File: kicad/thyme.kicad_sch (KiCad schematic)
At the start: 86 parts, among them SW1 SW_Push, SW10 SW_Push, SW11 SW_Push, SW12 SW_Push, SW13 SW_Push, SW14 SW_Push, SW15 SW_Push, SW16 SW_Push, SW17 SW_Push, SW18 SW_Push, SW19 SW_Push, SW2 SW_Push, SW20 SW_Push, SW21 SW_Push, SW22 SW_Push, SW23 SW_Push, SW24 SW_Push, SW25 SW_Push, SW26 SW_Push, SW27 SW_Push, SW28 SW_Push, SW29 SW_Push, SW3 SW_Push, SW30 SW_Push, SW31 SW_Push, SW32 SW_Push, SW33 SW_Push, SW34 SW_Push, SW35 SW_Push, SW36 SW_Push, SW37 SW_Push, SW38 SW_Push, SW39 SW_Push, SW4 SW_Push, SW40 SW_Push, SW41 SW_Push, SW42 SW_Push, SW5 SW_Push, SW6 SW_Push, SW7 SW_Push, SW8 SW_Push, SW9 SW_Push, U1 nice_nano, U2 nice_nano

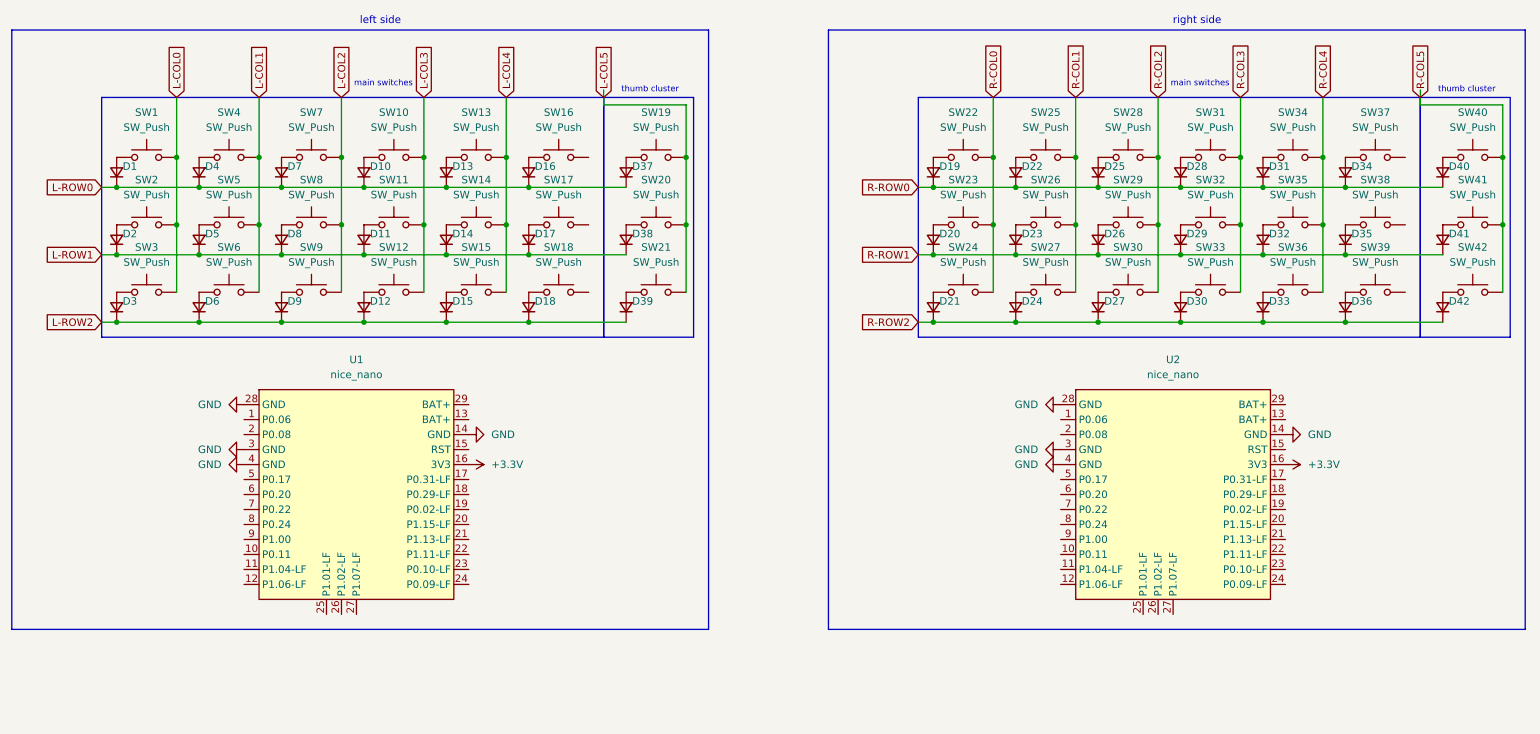
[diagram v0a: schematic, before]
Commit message: feat: add the jst power connections and connect nets
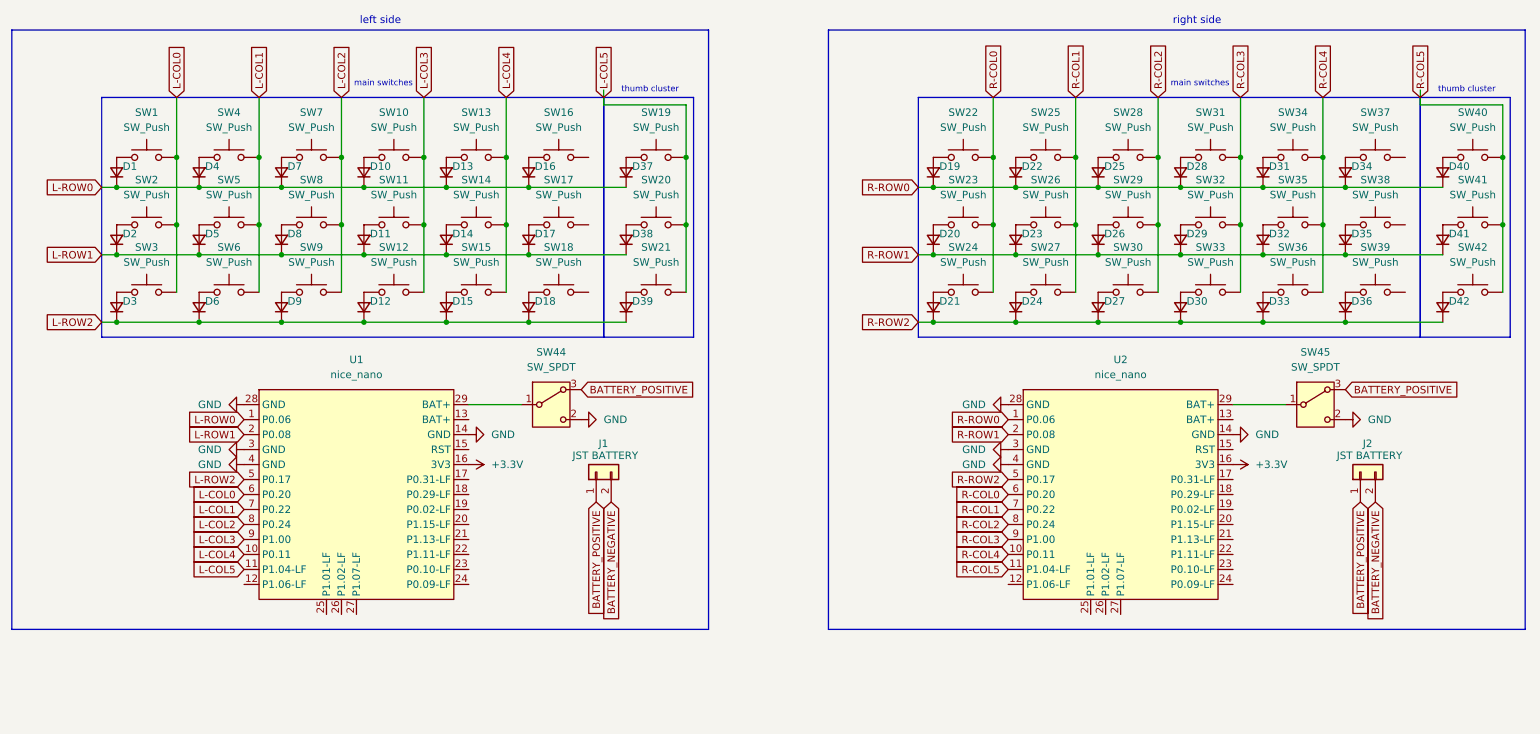
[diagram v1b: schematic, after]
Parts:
- added J1, J2: JST BATTERY, Connector_JST:JST_PH_B2B-PH-K_1x02_P2.00mm_Vertical, symbol Connector_Generic:Conn_01x02
- added SW44, SW45: SW_SPDT, Button_Switch_THT:SW_Slide-03_Wuerth-WS-SLTV_10x2.5x6.4_P2.54mm, symbol Switch:SW_Wuerth_450301014042
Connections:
- net GND: now also SW44.2 (C), SW45.2 (C)
- net L-COL0: now also U1.6 (P0.20)
- net L-COL1: now also U1.7 (P0.22)
- net L-COL2: now also U1.8 (P0.24)
- net L-COL3: now also U1.9 (P1.00)
- net L-COL4: now also U1.10 (P0.11)
- net L-COL5: now also U1.11 (P1.04-LF)
- net L-ROW0: now also U1.1 (P0.06)
- net L-ROW1: now also U1.2 (P0.08)
- net L-ROW2: now also U1.5 (P0.17)
- net R-COL0: now also U2.6 (P0.20)
- net R-COL1: now also U2.7 (P0.22)
- net R-COL2: now also U2.8 (P0.24)
- net R-COL3: now also U2.9 (P1.00)
- net R-COL4: now also U2.10 (P0.11)
- net R-COL5: now also U2.11 (P1.04-LF)
- net R-ROW0: now also U2.1 (P0.06)
- net R-ROW1: now also U2.2 (P0.08)
- net R-ROW2: now also U2.5 (P0.17)
- net at U1.29 (BAT+): now also SW44.1 (B)
- net at U2.29 (BAT+): now also SW45.1 (B)
- new net BATTERY_NEGATIVE: J1.2 (Pin_2), J2.2 (Pin_2)
- new net BATTERY_POSITIVE: J1.1 (Pin_1), J2.1 (Pin_1), SW44.3 (A), SW45.3 (A)

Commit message: bug: fix row 5 being unconnected
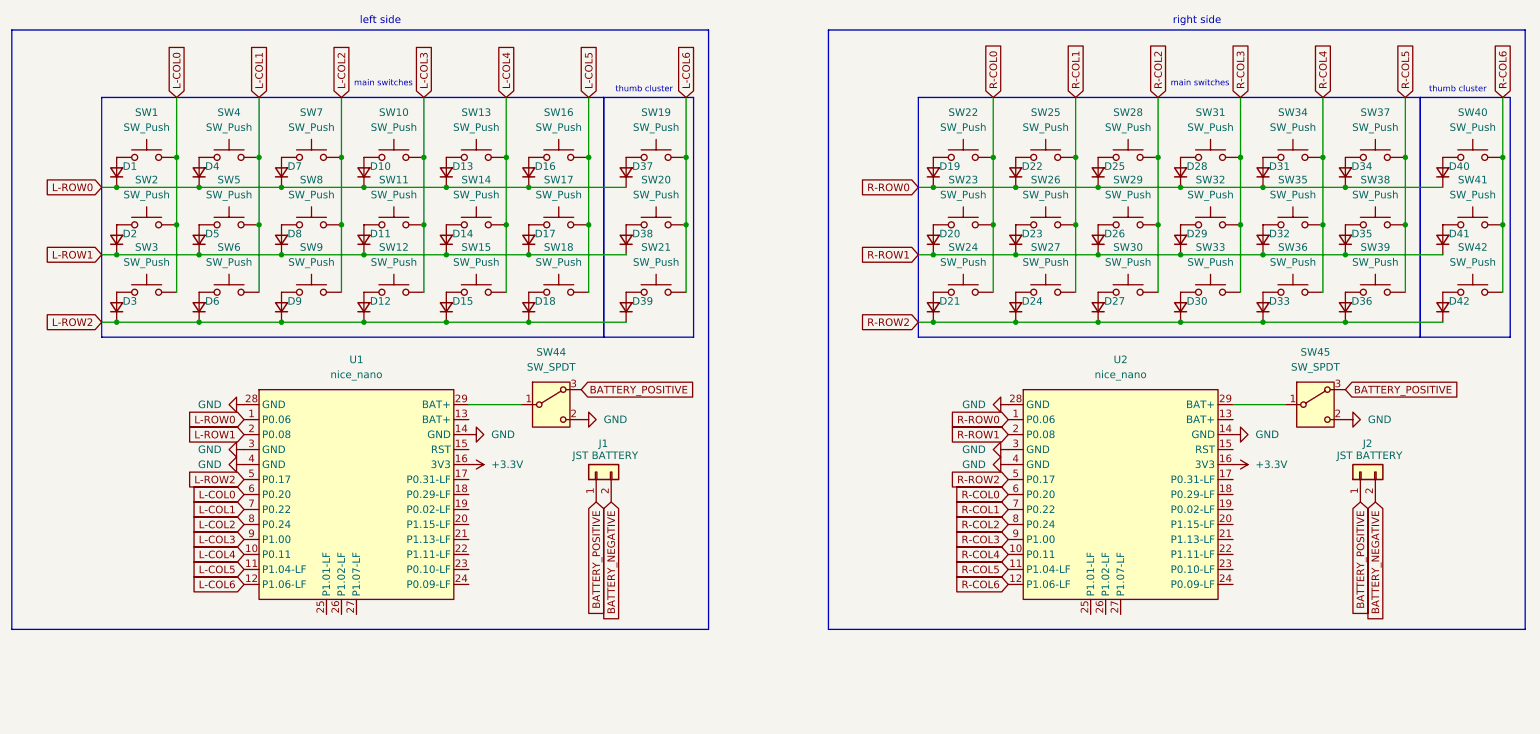
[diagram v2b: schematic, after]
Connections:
- net L-COL5: now also SW16.2, SW17.2, SW18.2; no longer SW19.2, SW20.2, SW21.2
- net R-COL5: now also SW37.2, SW38.2, SW39.2; no longer SW40.2, SW41.2, SW42.2
- net L-COL6: now reaches U1.12 (P1.06-LF)
- net L-COL6: now also SW19.2, SW20.2, SW21.2
- net R-COL6: now reaches U2.12 (P1.06-LF)
- net R-COL6: now also SW40.2, SW41.2, SW42.2

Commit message: chore: split power into left and right and add no connects
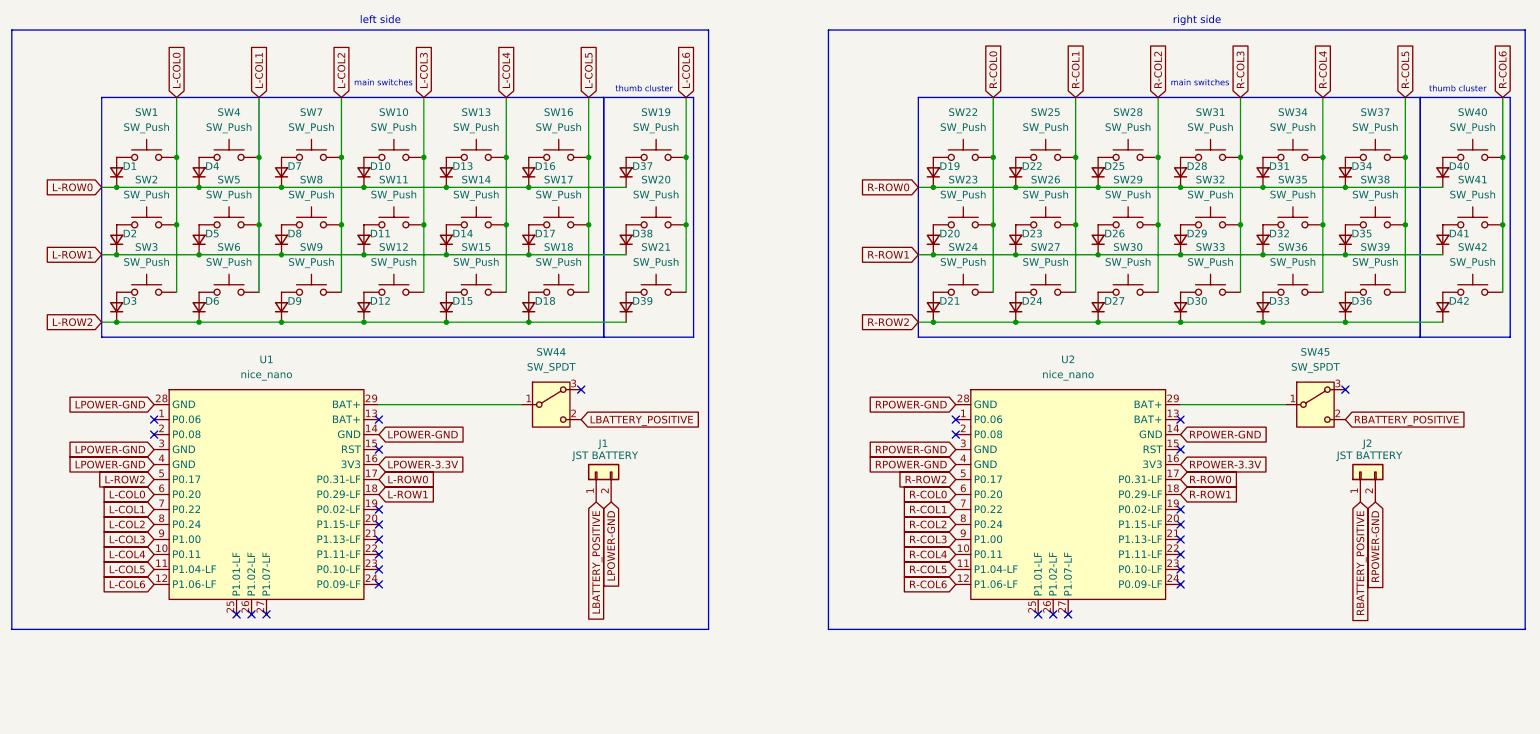
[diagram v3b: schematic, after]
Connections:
- net L-ROW0: now also U1.17 (P0.31-LF); no longer U1.1 (P0.06)
- net L-ROW1: now also U1.18 (P0.29-LF); no longer U1.2 (P0.08)
- net R-ROW0: now also U2.17 (P0.31-LF); no longer U2.1 (P0.06)
- net R-ROW1: now also U2.18 (P0.29-LF); no longer U2.2 (P0.08)
- net +3.3V renamed LPOWER-3.3V
- net LPOWER-3.3V: no longer U2.16 (3V3)
- net BATTERY_NEGATIVE renamed LPOWER-GND
- net LPOWER-GND: now also U1.14 (GND), U1.28 (GND), U1.3 (GND), U1.4 (GND); no longer J2.2 (Pin_2)
- removed net BATTERY_POSITIVE: J1.1 (Pin_1), J2.1 (Pin_1), SW44.3 (A), SW45.3 (A)
- removed net GND: SW44.2 (C), SW45.2 (C), U1.14 (GND), U1.28 (GND), U1.3 (GND), U1.4 (GND), U2.14 (GND), U2.28 (GND), U2.3 (GND), U2.4 (GND)
- new net LBATTERY_POSITIVE: J1.1 (Pin_1), SW44.2 (C)
- new net RBATTERY_POSITIVE: J2.1 (Pin_1), SW45.2 (C)
- new net RPOWER-3.3V: U2.16 (3V3)
- new net RPOWER-GND: J2.2 (Pin_2), U2.14 (GND), U2.28 (GND), U2.3 (GND), U2.4 (GND)
- no-connect marks 0 -> 28
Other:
- moved on the sheet: U1, U2

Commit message: feat: arrange switches and add edge cuts
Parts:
- J1, J2: footprint Connector_JST:JST_PH_B2B-PH-K_1x02_P2.00mm_Vertical -> Connector_JST:JST_PH_S2B-PH-SM4-TB_1x02-1MP_P2.00mm_Horizontal

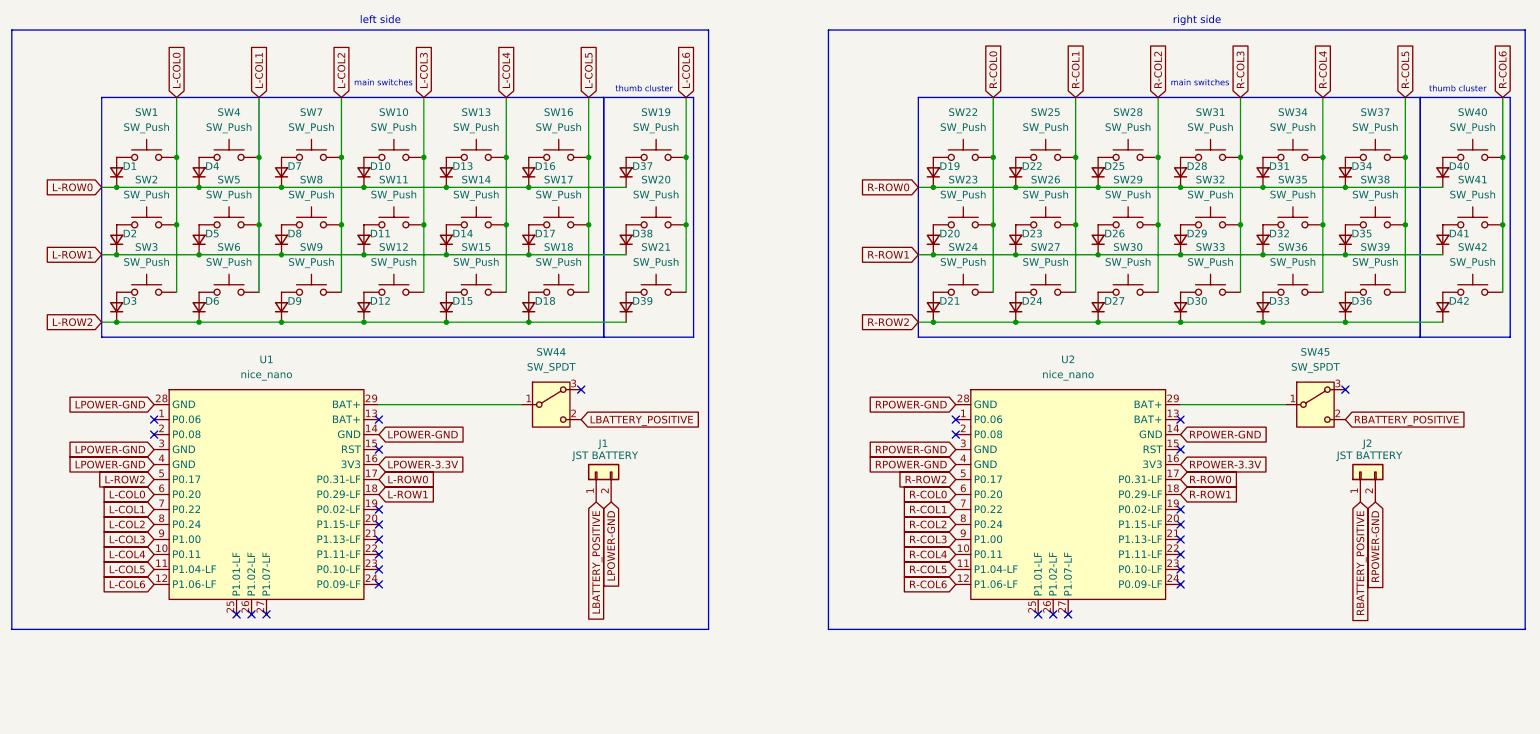
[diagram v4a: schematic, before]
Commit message: feat: add new jst connector and route the board
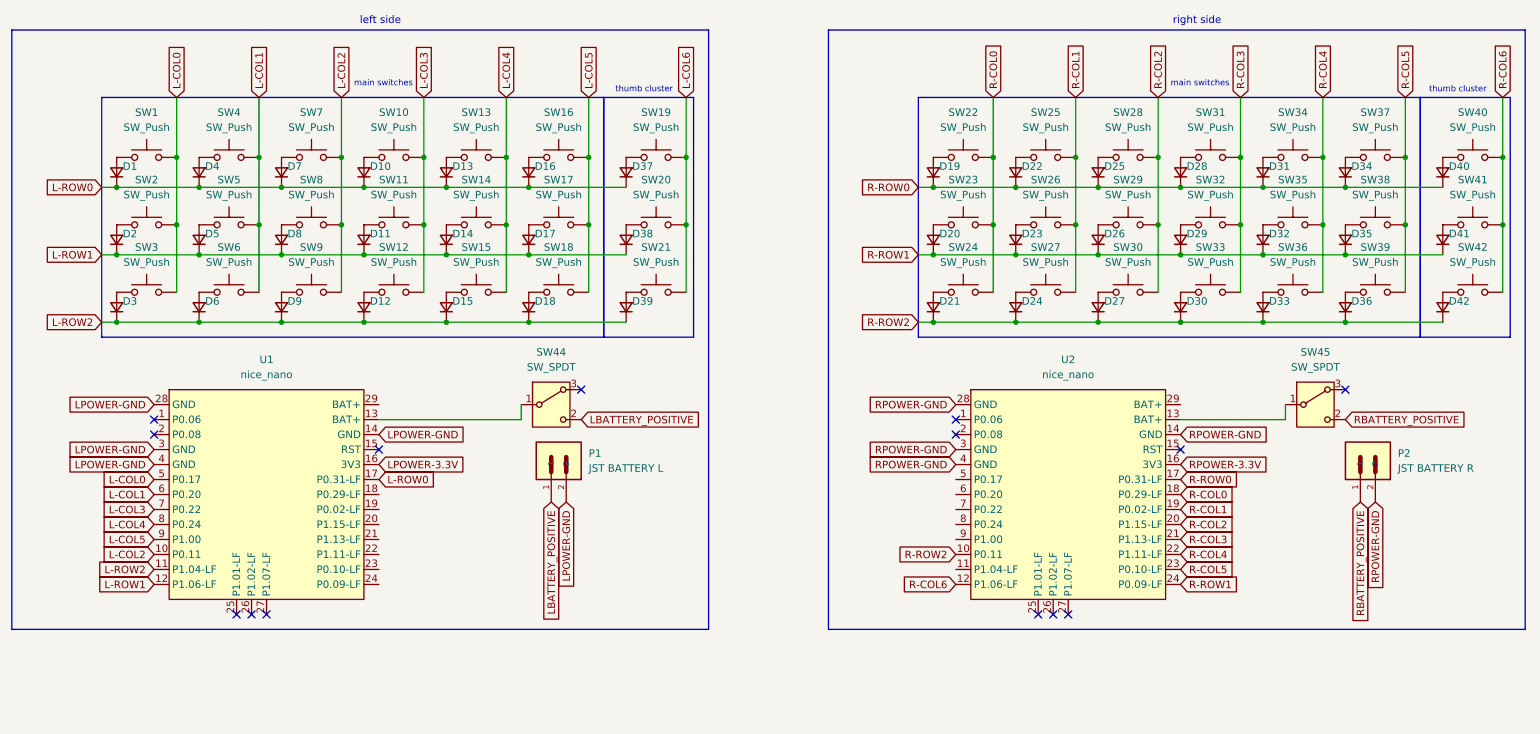
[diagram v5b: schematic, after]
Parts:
- removed J1, J2: JST BATTERY, Connector_JST:JST_PH_S2B-PH-SM4-TB_1x02-1MP_P2.00mm_Horizontal, symbol Connector_Generic:Conn_01x02
- added P1: JST BATTERY L, libraries:JST_S2B-PH-SM4-TB, symbol S2B-PH-SM4-TB:S2B-PH-SM4-TB
- added P2: JST BATTERY R, libraries:JST_S2B-PH-SM4-TB, symbol S2B-PH-SM4-TB:S2B-PH-SM4-TB
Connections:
- net L-COL0: now also U1.5 (P0.17); no longer U1.6 (P0.20)
- net L-COL1: now also U1.6 (P0.20); no longer U1.7 (P0.22)
- net L-COL2: now also U1.10 (P0.11); no longer U1.8 (P0.24)
- net L-COL3: now also U1.7 (P0.22); no longer U1.9 (P1.00)
- net L-COL4: now also U1.8 (P0.24); no longer U1.10 (P0.11)
- net L-COL5: now also U1.9 (P1.00); no longer U1.11 (P1.04-LF)
- net L-COL6: no longer U1.12 (P1.06-LF)
- net L-ROW1: now also U1.12 (P1.06-LF); no longer U1.18 (P0.29-LF)
- net L-ROW2: now also U1.11 (P1.04-LF); no longer U1.5 (P0.17)
- net LBATTERY_POSITIVE: now also P1.1
- net LPOWER-GND: now also P1.2
- net R-COL0: now also U2.18 (P0.29-LF); no longer U2.6 (P0.20)
- net R-COL1: now also U2.19 (P0.02-LF); no longer U2.7 (P0.22)
- net R-COL2: now also U2.20 (P1.15-LF); no longer U2.8 (P0.24)
- net R-COL3: now also U2.21 (P1.13-LF); no longer U2.9 (P1.00)
- net R-COL4: now also U2.22 (P1.11-LF); no longer U2.10 (P0.11)
- net R-COL5: now also U2.23 (P0.10-LF); no longer U2.11 (P1.04-LF)
- net R-ROW1: now also U2.24 (P0.09-LF); no longer U2.18 (P0.29-LF)
- net R-ROW2: now also U2.10 (P0.11); no longer U2.5 (P0.17)
- net RBATTERY_POSITIVE: now also P2.1
- net RPOWER-GND: now also P2.2
- net at U1.13 (BAT+): now also SW44.1 (B)
- net at U1.29 (BAT+): no longer SW44.1 (B)
- net at SW45.1 (B): now also U2.13 (BAT+); no longer U2.29 (BAT+)
- no-connect marks 28 -> 14

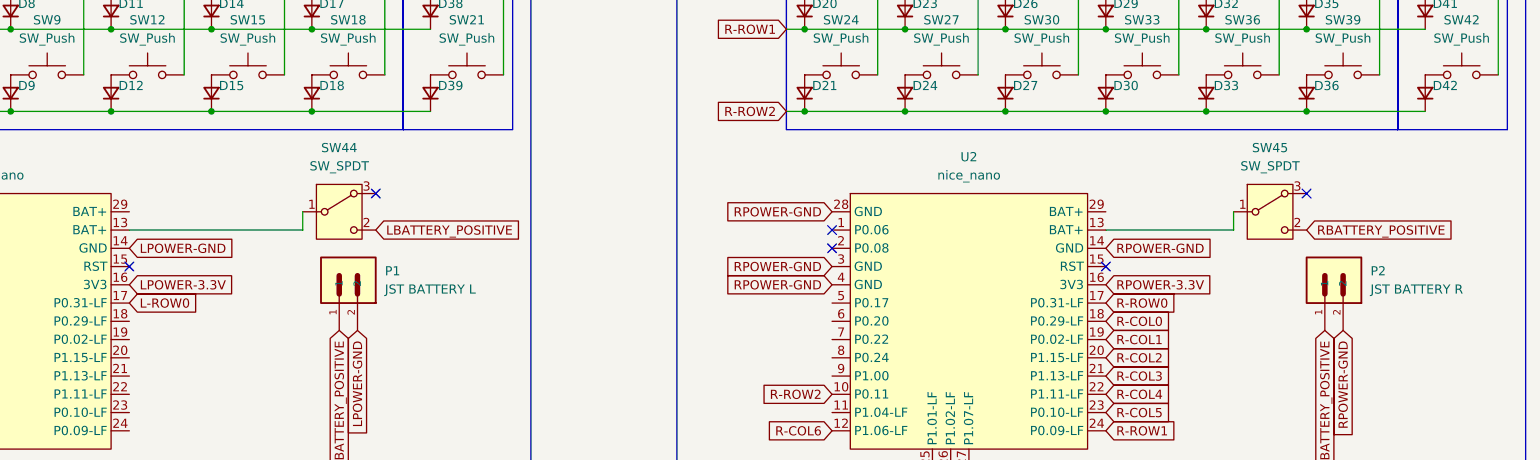
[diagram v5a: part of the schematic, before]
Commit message: feat: move to jst tht connector and new switches
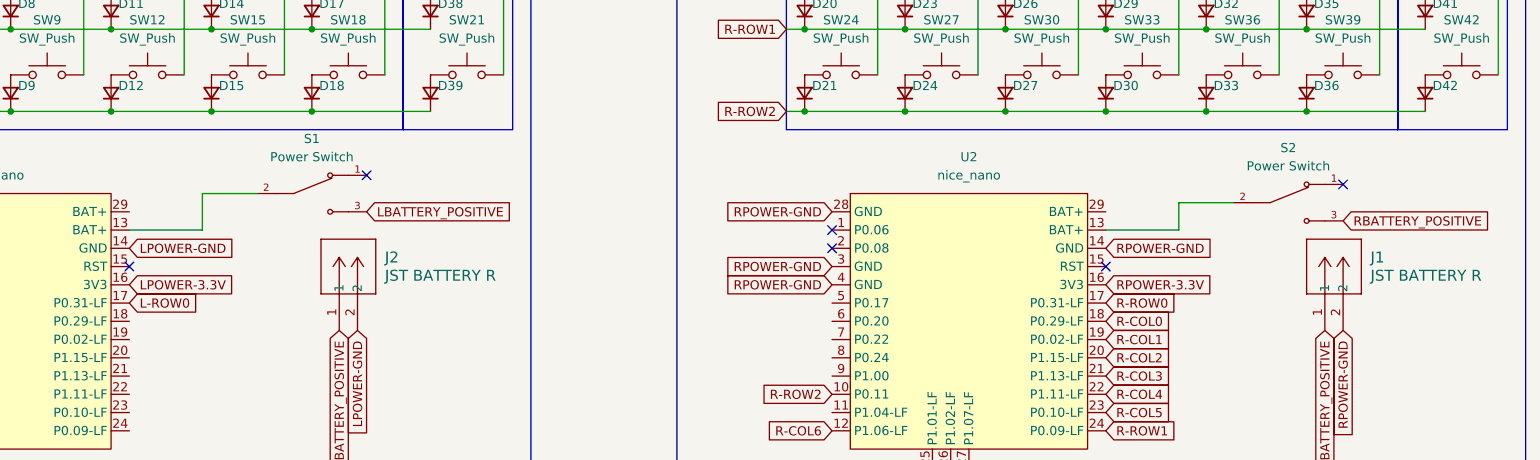
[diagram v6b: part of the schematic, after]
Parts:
- removed P1: JST BATTERY L, libraries:JST_S2B-PH-SM4-TB, symbol S2B-PH-SM4-TB:S2B-PH-SM4-TB
- removed P2: JST BATTERY R, libraries:JST_S2B-PH-SM4-TB, symbol S2B-PH-SM4-TB:S2B-PH-SM4-TB
- removed SW44, SW45: SW_SPDT, Button_Switch_THT:SW_Slide-03_Wuerth-WS-SLTV_10x2.5x6.4_P2.54mm, symbol Switch:SW_Wuerth_450301014042
- added J1, J2: JST BATTERY R, libraries:CONN_S2B-PH-K-S_JST, symbol S2B-PH-K-S:S2B-PH-K-SLFSN
- added S1, S2: Power Switch, libraries:SW_SLW-1277744-3A-N-D, symbol SLW-1277744-3A-N-D:SLW-1277744-3A-N-D
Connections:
- net LBATTERY_POSITIVE: now also J2.1, S1.3
- net LPOWER-GND: now also J2.2
- net RBATTERY_POSITIVE: now also J1.1, S2.3
- net RPOWER-GND: now also J1.2
- net at U1.13 (BAT+): now also S1.2
- net at U2.13 (BAT+): now also S2.2
